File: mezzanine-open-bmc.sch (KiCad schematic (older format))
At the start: 50 parts, among them P1 CONN_02X20, P2 CONN_02X20, Q1 S8050, Q2 S8050, SW1 PWR, SW2 RST, U1 FT230XS, U2 PMIC-CJT1117-3.3(SOT223), U3 DS3231N, U4 PCA9306, U5 M24C16-WMN6P

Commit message: Wire Up BB LED (1.8v)
The wiring for the LED components of 1.8 have been connnected up in a neat little
bundle which can be placed on the board.

Signed-off-by: Sophie Haynes <sophie.haynes@linaro.org>
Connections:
- net labels removed: GPIO_I_BMC, GPIO_J_BMC, GPIO_K_BMC, GPIO_L_BMC
- wire segments 241 -> 237
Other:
- note removed: "Connect GPIO"
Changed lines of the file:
@@
 GPIO_G_BMC
 Text GLabel 3900 2500 0    60   Input ~ 0
-GPIO_I_BMC
+GPIO_I
 Text GLabel 3900 2600 0    60   Input ~ 0
-GPIO_K_BMC
+GPIO_K
 Text GLabel 3900 1600 0    60   Input ~ 0
 UART1_RX_BMC
@@
 GPIO_H_BMC
 Text GLabel 4650 2500 2    60   Input ~ 0
-GPIO_J_BMC
+GPIO_J
 Text GLabel 4650 2600 2    60   Input ~ 0
-GPIO_L_BMC
+GPIO_L
 $Comp
 L GND #PWR07
@@
 Text Notes 4450 7600 0    60   ~ 0
 BMC PWR LED's
-Text GLabel 4800 3400 0    60   Input ~ 0
-GPIO_I
-Text GLabel 4800 3650 0    60   Input ~ 0
-GPIO_K
-Text GLabel 5100 3400 2    60   Input ~ 0
-GPIO_I_BMC
-Text GLabel 5100 3650 2    60   Input ~ 0
-GPIO_K_BMC
-Text GLabel 4800 3900 0    60   Input ~ 0
-GPIO_J
-Text GLabel 4800 4150 0    60   Input ~ 0
-GPIO_L
-Text GLabel 5100 3900 2    60   Input ~ 0
-GPIO_J_BMC
-Text GLabel 5100 4150 2    60   Input ~ 0
-GPIO_L_BMC
-Text Notes 4700 4400 0    60   ~ 0
-Connect GPIO
 $Comp
 L FT230XS U1
@@
 Wire Notes Line
 	3650 5500 3650 7700
-Wire Wire Line
-	4800 3400 5100 3400
-Wire Wire Line
-	4800 3650 5100 3650
-Wire Wire Line
-	4800 3900 5100 3900
-Wire Wire Line
-	4800 4150 5100 4150
 Wire Notes Line
 	4500 4500 5700 4500
@@
 	7400 4500 7400 5300
 Wire Notes Line
-	4350 4400 4350 3250
-Wire Notes Line
 	5850 3200 5850 4350

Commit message: Grant Tweaks
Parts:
- removed D2, D6: Led_Small, LEDs:LED_0603, symbol Led_Small
- removed Q1, Q2: S8050, 96boards:SOT-23_Seeed, symbol S8050
- removed R12: 22R, Resistors_SMD:R_0603, symbol R
- removed R14: 1k, Resistors_SMD:R_0603, symbol R
- removed R15: 10k, Resistors_SMD:R_0603, symbol R
- removed R16, R9: 390R, Resistors_SMD:R_0603, symbol R
- C5, C7: footprint (none) -> Capacitors_SMD:C_0603
- R18, R19: value 2.2K Ω -> 2.2K
- R4: value 22R -> 10k
- R5, R6: value 220R -> 22R
- R7: value 1k -> 0R
- R8: value 10k -> 0R
- U2: footprint 96boards:SOT-223 -> TO_SOT_Packages_SMD:SOT-223; symbol PMIC-CJT1117-3.3(SOT223) -> AP1117
- U3: footprint (none) -> SMD_Packages:SO-16-W
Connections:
- net labels removed: UART0_CTS_BMC, UART0_RTS_BMC, UART0_RX_BMC, UART0_TX_BMC
- wire segments 237 -> 221
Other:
- note removed: "BB UART1 to BMC UART0"
- moved on the sheet: C10, C5, C6, C7, D7, R11, R17

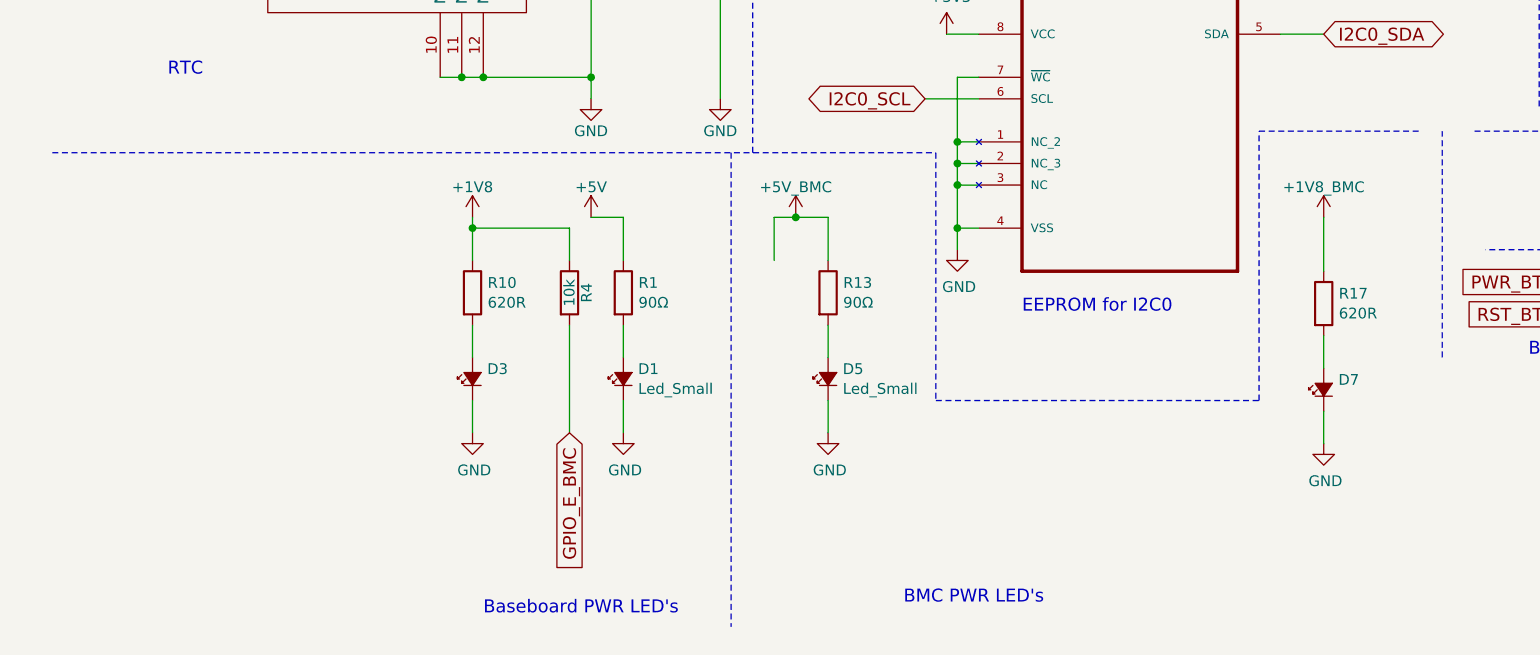
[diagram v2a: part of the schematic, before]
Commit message: Tidy LED (Schematic)
LED's have been moved and wires aligned.

Signed-off-by: Sophie Haynes <sophie.haynes@linaro.org>
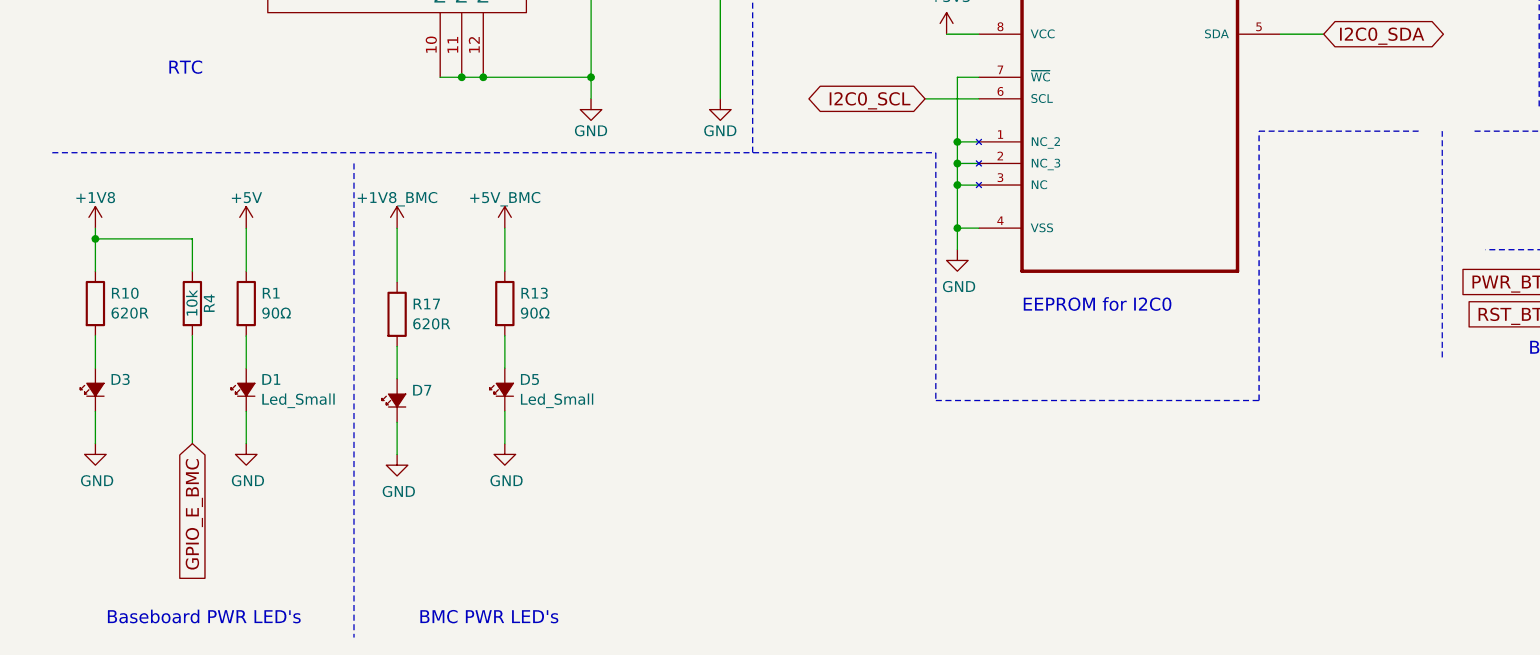
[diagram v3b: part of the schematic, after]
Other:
- moved on the sheet: D1, D3, D5, D7, R1, R10, R13, R17, R4

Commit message: Add Grove Connectors for I2C
The two I2C lines have now been wired to two grove connectors and passed
through level shifter to 5v

Signed-off-by: Sophie Haynes <sophie.haynes@linaro.org>
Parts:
- added C12, C13: 1uF, Capacitors_SMD:C_0603, symbol C_Small
- added C? (x2): 100n, Capacitors_SMD:C_0603, symbol C_Small
- added P? (x2): CONN_01X04, symbol CONN_01X04
- added U6: REG_1.8V, 96boards:SOT-23_Seeed, symbol LM317AEMP
- added U?: TXS0104PW, symbol TXS0104PW
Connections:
- net labels added: +3V3_F, I2C0_SCL/5, I2C0_SDA/5, I2C1_SCL/5, I2C1_SDA/5
- wire segments 218 -> 250

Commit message: Connect Up Components
All components are connected (barring the battery since there is no
footprint currently)

Signed-off-by: Sophie Haynes <sophie.haynes@linaro.com>
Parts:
- P3, P4: renamed from P?; footprint (none) -> 96boards:Grove4P
- U7: renamed from U?; footprint (none) -> Housings_SSOP:SSOP-14_5.3x6.2mm_Pitch0.65mm
- gave numbers to parts that had none: 2
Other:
- moved on the sheet: C10, C11, C14, C15, C3, C4, C5, C6, C7, C9, CON1, R11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

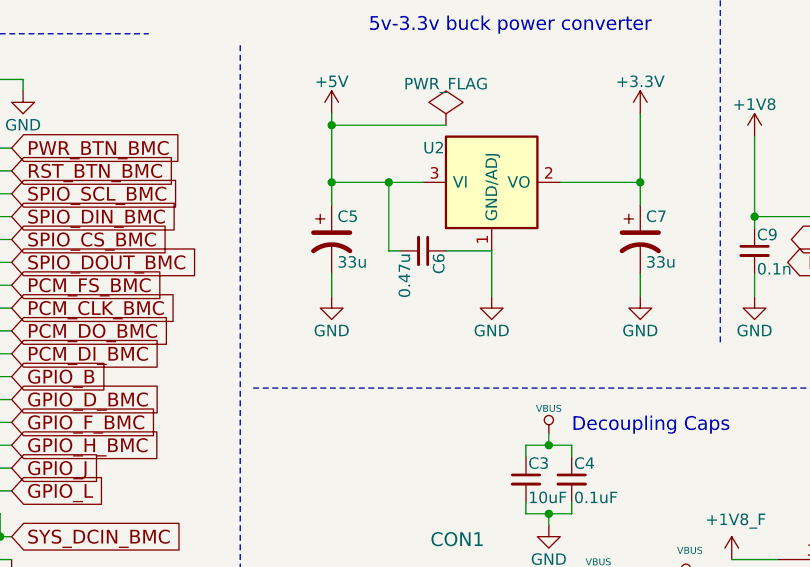
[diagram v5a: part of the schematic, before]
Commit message: Complete PCB Layout and Include Missing Footprints (BT1, C5, C7)
The missing footprints have been added to both the schematic and the PCB.
Capacitor values for C6 have been changes to 0.1uF.
The new components have been connected up in the PCB.

Signed-off-by: Sophie Haynes <sophie.haynes@linaro.org>
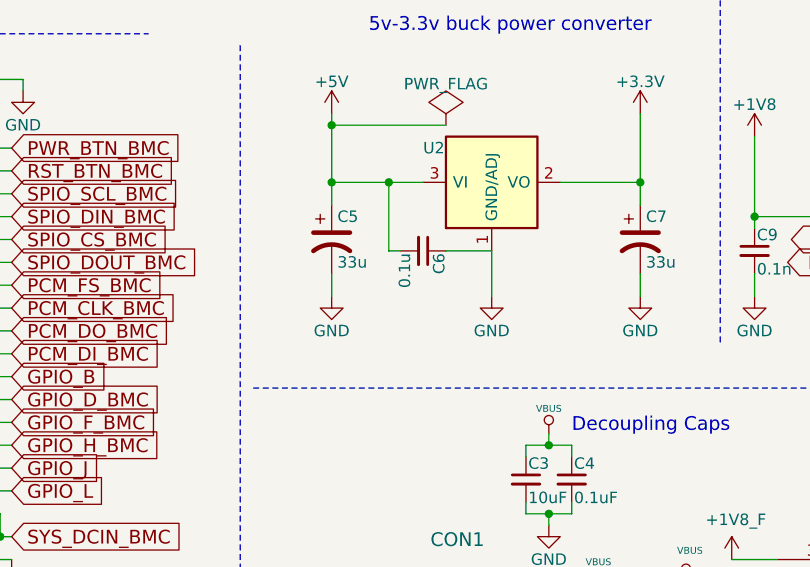
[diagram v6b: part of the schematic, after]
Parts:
- BT1: footprint (none) -> Connect:CR2032H
- C5, C7: footprint Capacitors_SMD:C_0603 -> Capacitors_SMD:C_1206
- C6: value 0.47u -> 0.1u
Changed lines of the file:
@@
 F 0 "BT1" H 3700 4400 50  0000 L CNN
 F 1 "Battery CR2032" H 3700 4300 50  0000 L CNN
-F 2 "" V 3600 4390 50  0001 C CNN
+F 2 "Connect:CR2032H" V 3600 4390 50  0001 C CNN
 F 3 "" V 3600 4390 50  0000 C CNN
 	1    3600 4350
@@
 F 0 "C5" H 6075 1600 50  0000 L CNN
 F 1 "33u" H 6075 1400 50  0000 L CNN
-F 2 "Capacitors_SMD:C_0603" H 6050 1500 50  0001 C CNN
+F 2 "Capacitors_SMD:C_1206" H 6050 1500 50  0001 C CNN
 F 3 "" H 6050 1500 50  0000 C CNN
 	1    6050 1500
@@
 P 6450 1550
 F 0 "C6" H 6460 1620 50  0000 L CNN
-F 1 "0.47u" H 6460 1470 50  0000 L CNN
+F 1 "0.1u" H 6460 1470 50  0000 L CNN
 F 2 "Capacitors_SMD:C_0603" H 6450 1550 50  0001 C CNN
 F 3 "" H 6450 1550 50  0000 C CNN
@@
 F 0 "C7" H 7425 1600 50  0000 L CNN
 F 1 "33u" H 7425 1400 50  0000 L CNN
-F 2 "Capacitors_SMD:C_0603" H 7400 1500 50  0001 C CNN
+F 2 "Capacitors_SMD:C_1206" H 7400 1500 50  0001 C CNN
 F 3 "" H 7400 1500 50  0000 C CNN
 	1    7400 1500

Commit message: Change Grove Connectors to SMD
Since this is a stacking board, it would be difficult to access
upright connectors. Therefore. they have been changed to right angled grove
connectors.

Signed-off-by: Sophie Haynes <sophie.haynes@linaro.org>
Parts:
- removed U7: TXS0104PW, Housings_SSOP:SSOP-14_5.3x6.2mm_Pitch0.65mm, symbol TXS0104PW
- added C16, C17: 0.1n, Capacitors_SMD:C_0603, symbol C_Small
- added P5: CONN_01X04, 96boards:Grove_SMD_Connector, symbol CONN_01X04
- added R12, R14, R15, R9: 2.2K, Resistors_SMD:R_0603, symbol 220R
- added R16, R21: 200k, Resistors_SMD:R_0603, symbol R_Small
- added R22: 0R, Resistors_SMD:R_1206, symbol R
- added U7, U8: PCA9306, 96boards:PCA9306, symbol PCA9306
- C14, C15: value 100n -> 0.1n; Seeed SKU 302010139 -> (none)
- P3, P4: footprint 96boards:Grove4P -> 96boards:Grove_SMD_Connector
- R1, R13: value 90Ω -> 990R
- R10, R17: value 620R -> 22R
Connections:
- net labels added: I2C1_SCL_3.3, I2C1_SCL_BMC_3.3, I2C1_SDA_3.3, I2C1_SDA_BMC_3.3
- net labels removed: I2C0_SCL/5, I2C0_SDA/5, I2C1_SCL/5, I2C1_SDA/5
- wire segments 250 -> 278
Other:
- moved on the sheet: C6, R7, R8, SW1, SW2

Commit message: Make Layout in SCH Pretty
Grove connector layout have been redrawn into a heirarhcial sheet.

Signed-off-by: Sophie Haynes <sophie.haynes@linaro.org>
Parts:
- removed C10, C14, C15, C16, C17, C9: 0.1n, Capacitors_SMD:C_0603, symbol C_Small
- removed R11, R16, R21: 200k, Resistors_SMD:R_0603, symbol R_Small
- removed R12, R14, R15, R18, R19, R9: 2.2K, Resistors_SMD:R_0603, symbol 220R
- removed U4, U7, U8: PCA9306, 96boards:PCA9306, symbol PCA9306
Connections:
- net USB+: now reaches R6.1, U1.8 (USBD+)
- net USB+: now also C1.1, CON1.3 (D+), R6.2
- net USB-: now reaches R5.1, U1.9 (USBD-)
- net USB-: now also C2.1, CON1.2 (D-), R5.2
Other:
- note removed: "1.8v-3.3v level shifter"
- moved on the sheet: C1, C11, C12, C13, C2, C3, C4, C5, C6, C7, CON1, P3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
